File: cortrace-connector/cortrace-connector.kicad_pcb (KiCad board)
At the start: 2 copper layers, 8 parts, among them J1 FPGA-PORT, J2 Conn_ARM_Cortex_Debug_ETM_20, J4 SWD-PORT

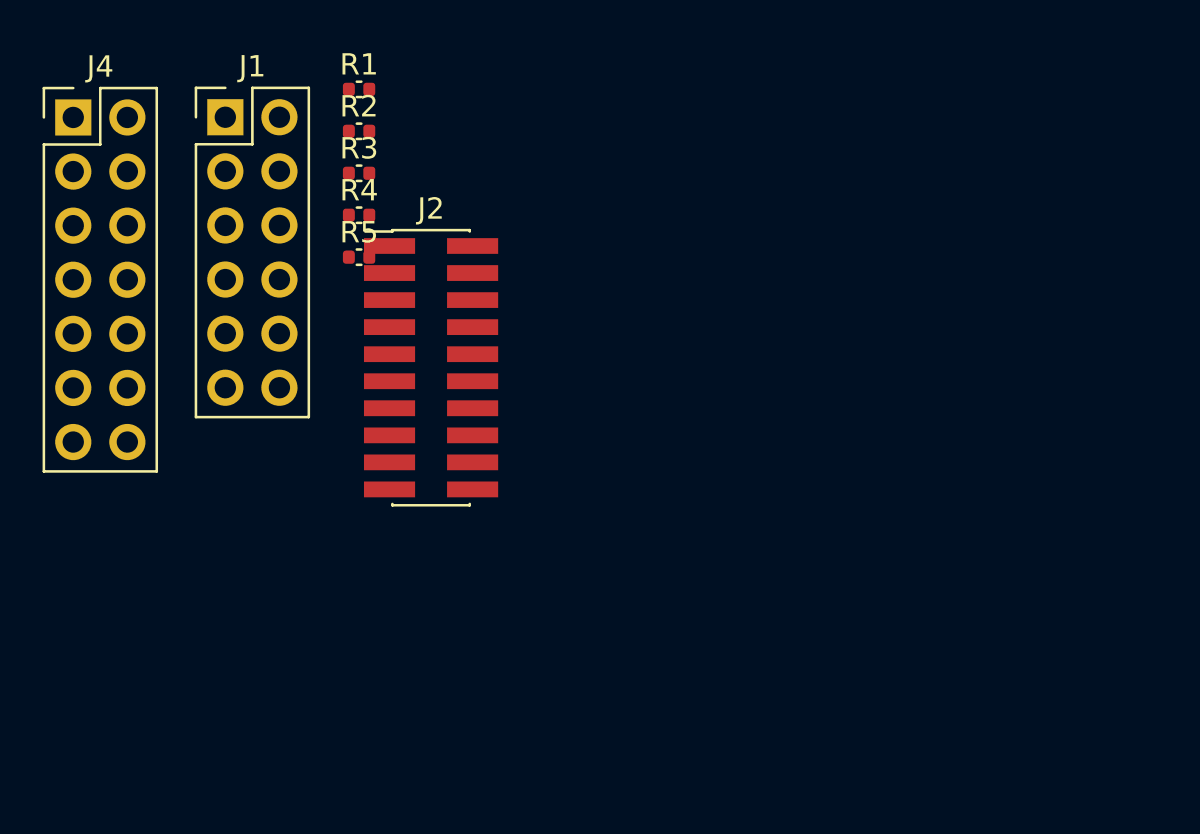
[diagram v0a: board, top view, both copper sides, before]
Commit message: feat(connector): lay out and route the adapter board
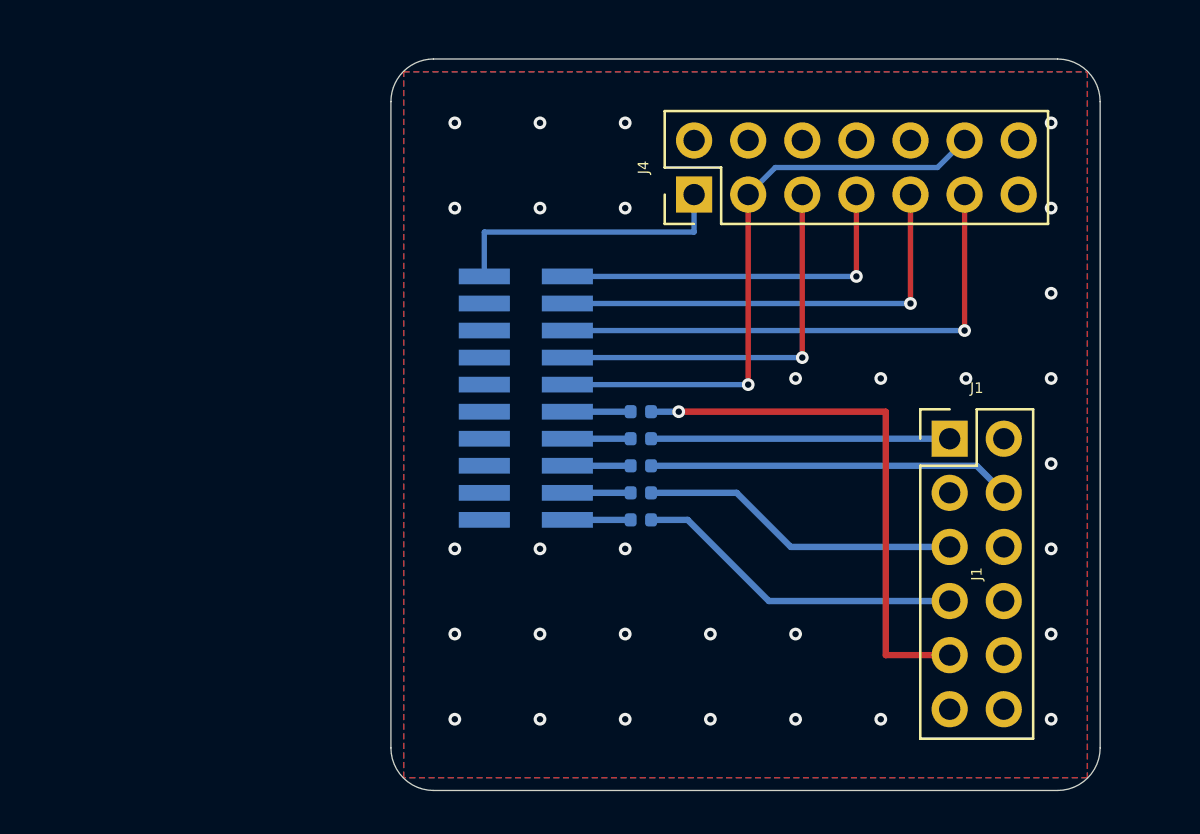
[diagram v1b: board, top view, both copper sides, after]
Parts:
- J2, R1, R2, R3, R4, R5: moved to B.Cu
- moved J1 37.2 mm to (140.0, 81.9)
- moved J4 29.4 mm to (128.0, 70.4), turned to 90 degrees
- moved R1 20.1 mm to (125.5, 80.6)
- moved R2 19.6 mm to (125.5, 81.9)
- moved R3 19.1 mm to (125.5, 83.2)
- moved R4 18.6 mm to (125.5, 84.4)
- moved R5 18.1 mm to (125.5, 85.7)
- moved J2 4.67 mm to (120.1, 80.0), turned to 180 degrees
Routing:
- net /NRST: track 0.00 -> 28.6 mm, vias 0 -> 1
- net /TRACE-CLK: track 0.00 -> 25.4 mm, vias 0 -> 1
- net /TDO: track 0.00 -> 25.0 mm, vias 0 -> 1
- net /TCK: track 0.00 -> 21.2 mm, vias 0 -> 1
- net /TDI: track 0.00 -> 18.7 mm, vias 0 -> 1
- net /TMS: track 0.00 -> 17.4 mm, vias 0 -> 1
- net /TRACE-D1: track 0.00 -> 17.1 mm
- net /TRACE-D3: track 0.00 -> 15.6 mm
- net /TRACE-D2: track 0.00 -> 15.1 mm
- net /TRACE-D0: track 0.00 -> 14.0 mm
- net /VREF: track 0.00 -> 13.7 mm
- net Net-(J2-TRACEDATA3): track 0.00 -> 2.97 mm
- net Net-(J2-TRACEDATA2): track 0.00 -> 2.97 mm
- net Net-(J2-TRACEDATA1): track 0.00 -> 2.97 mm
- net Net-(J2-TRACEDATA0): track 0.00 -> 2.97 mm
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- added copper zone on B.Cu, net GND
- added copper zone on F.Cu, net GND
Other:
- board outline added: 33.3 x 34.3 mm

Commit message: feat(connector): re-lay out the adapter board with arc routing
Import the board rules from DutyCycle, follow the sketched placement (TRACE socket left, JTAG and FPGA headers right), route every signal on B.Cu with arcs and no vias, add teardrops, GND pours, stitching vias and silkscreen (logo, author, revision, date, pin names).
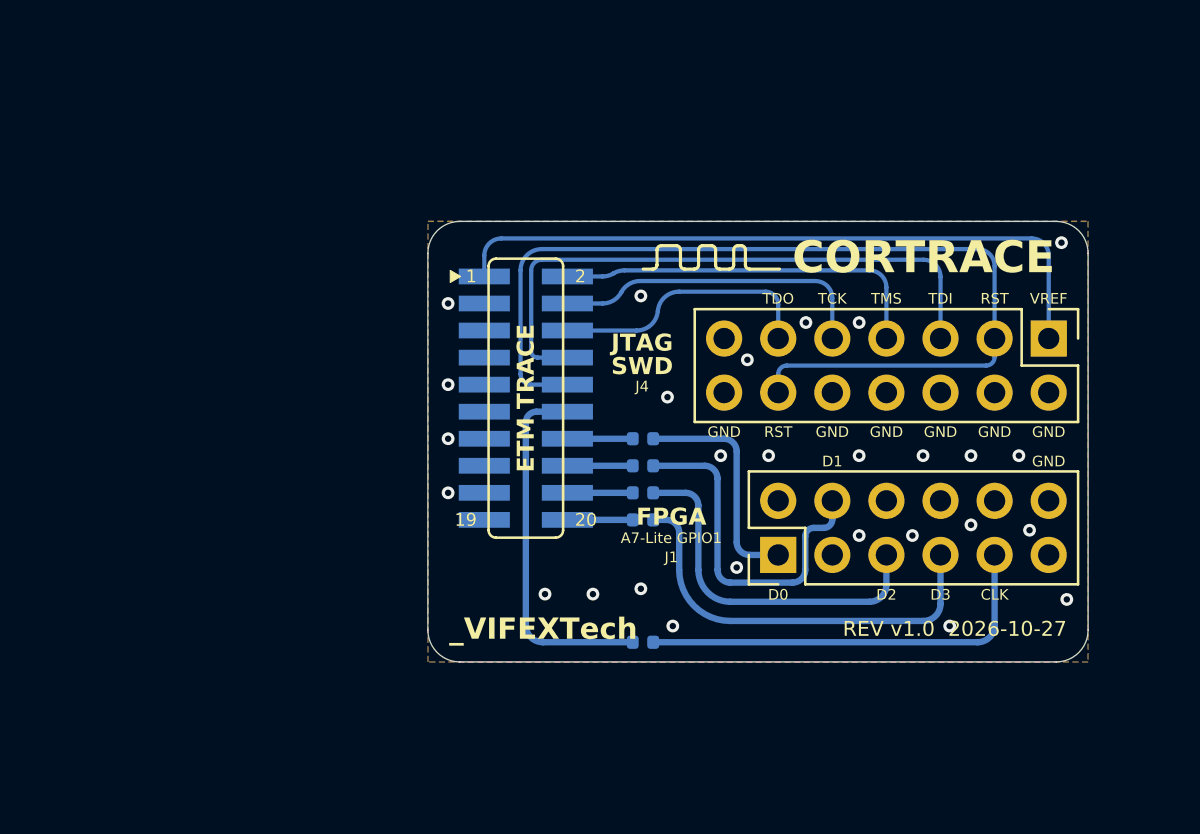
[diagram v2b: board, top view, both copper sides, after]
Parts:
- moved J4 18.0 mm to (144.7, 77.2), turned to -90 degrees
- moved R1 10.8 mm to (125.6, 91.5)
- moved J1 9.72 mm to (131.9, 87.4), turned to 90 degrees
- moved R2 0.10 mm to (125.6, 81.9)
- moved R3 0.10 mm to (125.6, 83.2)
- moved R4 0.10 mm to (125.6, 84.4)
- moved R5 0.10 mm to (125.6, 85.7)
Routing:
- net /VREF: track 13.7 -> 32.2 mm
- net /NRST: track 28.6 -> 46.3 mm, vias 1 -> 0
- net Net-(J2-TRACECLK): track 2.97 -> 17.2 mm
- net /TDO: track 25.0 -> 12.7 mm, vias 1 -> 0
- net /TDI: track 18.7 -> 28.5 mm, vias 1 -> 0
- net /TCK: track 21.2 -> 15.1 mm, vias 1 -> 0
- net /TRACE-CLK: track 25.4 -> 19.8 mm, vias 1 -> 0
- net /TRACE-D3: track 15.6 -> 19.6 mm
- net /TRACE-D0: track 14.0 -> 10.8 mm
- net /TRACE-D2: track 15.1 -> 16.9 mm
- net /TRACE-D1: track 17.1 -> 16.5 mm
- net /TMS: track 17.4 -> 17.9 mm, vias 1 -> 0
- net GND: vias 31 -> 27
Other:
- board size 33.3 x 34.3 mm -> 31 x 20.7 mm
- board text added: "1"
- board text added: "19"
- board text added: "2"
- board text added: "20"
- board text added: "A7-Lite GPIO1"
- board text added: "CLK"
- board text added: "CORTRACE"
- board text added: "D0"
- board text added: "D1"
- board text added: "D2"
- board text added: "D3"
- board text added: "ETM TRACE"
- board text added: "FPGA"
- board text added: "GND"
- board text added: "JTAG"
- board text added: "REV ${REVISION} ${ISSUE_DATE}"
- board text added: "RST"
- board text added: "SWD"
- board text added: "TCK"
- board text added: "TDI"
- board text added: "TDO"
- board text added: "TMS"
- board text added: "TRACE"
- board text added: "VREF"
- board text added: "_VIFEXTech"

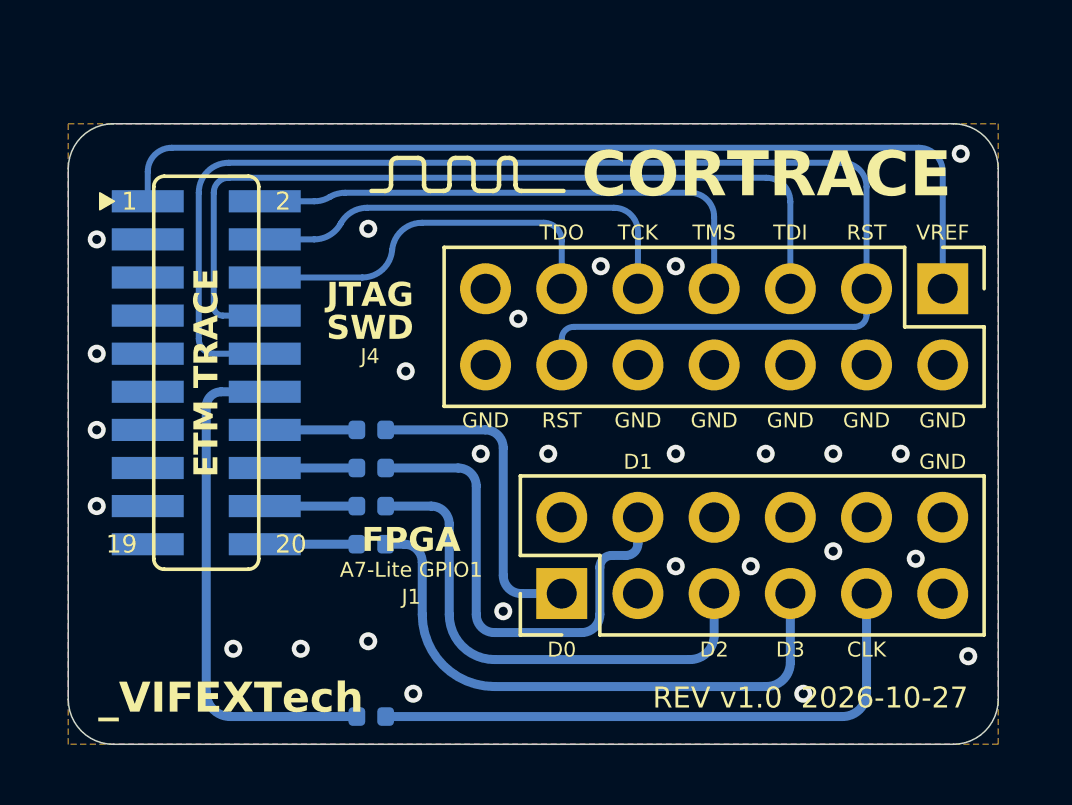
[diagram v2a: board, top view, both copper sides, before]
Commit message: feat(connector): length-match the TRACE nets and centre the board on J2
All five TRACE nets (J2 pad to J1 pad) are 24.174 mm. CLK now runs straight through the gap between the headers; D0..D3 are tuned with rounded bumps and a trombone, each in space only that net reaches. The outline is symmetric about the J2 centre.
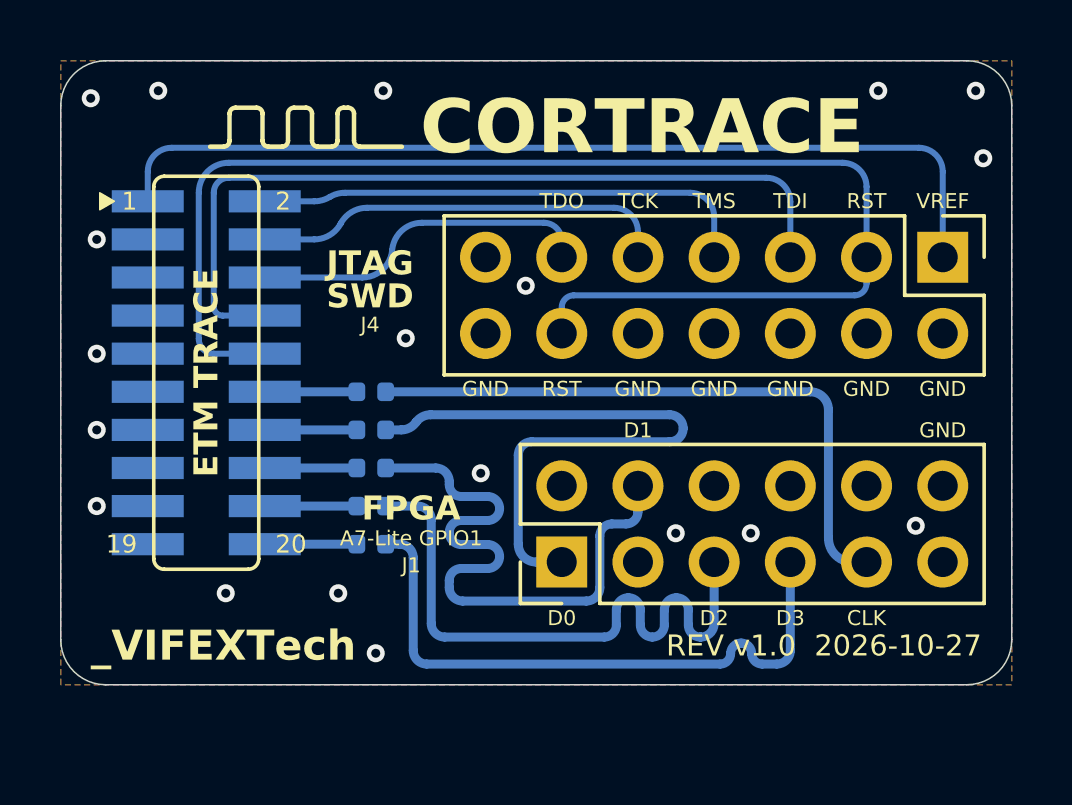
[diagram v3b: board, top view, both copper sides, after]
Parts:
- moved R1 10.8 mm to (125.6, 80.6)
- moved J1 1.05 mm to (131.9, 86.3)
- moved J4 1.05 mm to (144.7, 76.2)
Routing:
- net Net-(J2-TRACECLK): track 17.2 -> 3.07 mm
- net /TRACE-D0: track 10.8 -> 21.0 mm
- net /TRACE-D1: track 16.5 -> 20.9 mm
- net /TRACE-D2: track 16.9 -> 20.9 mm
- net /TRACE-D3: track 19.6 -> 21.0 mm
- net /TRACE-CLK: track 19.8 -> 21.0 mm
- net /TMS: track 17.9 -> 16.8 mm
- net /TDO: track 12.7 -> 11.7 mm
- net /TDI: track 28.5 -> 27.4 mm
- net /TCK: track 15.1 -> 14.1 mm
- net /VREF: track 32.2 -> 31.2 mm
- net /NRST: track 46.3 -> 45.2 mm
- net GND: vias 27 -> 19
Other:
- board size 31 x 20.7 mm -> 31.7 x 20.8 mm

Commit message: feat(connector): label the SWD pin names on the debug header
TMS/SWDIO, TCK/SWCLK and TDO/SWO share a pin each, so the silkscreen shows both names on two lines. VREF and RST apply to both modes.
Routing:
- net GND: vias 19 -> 18
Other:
- board text added: "SWCLK"
- board text added: "SWDIO"
- board text added: "SWO"

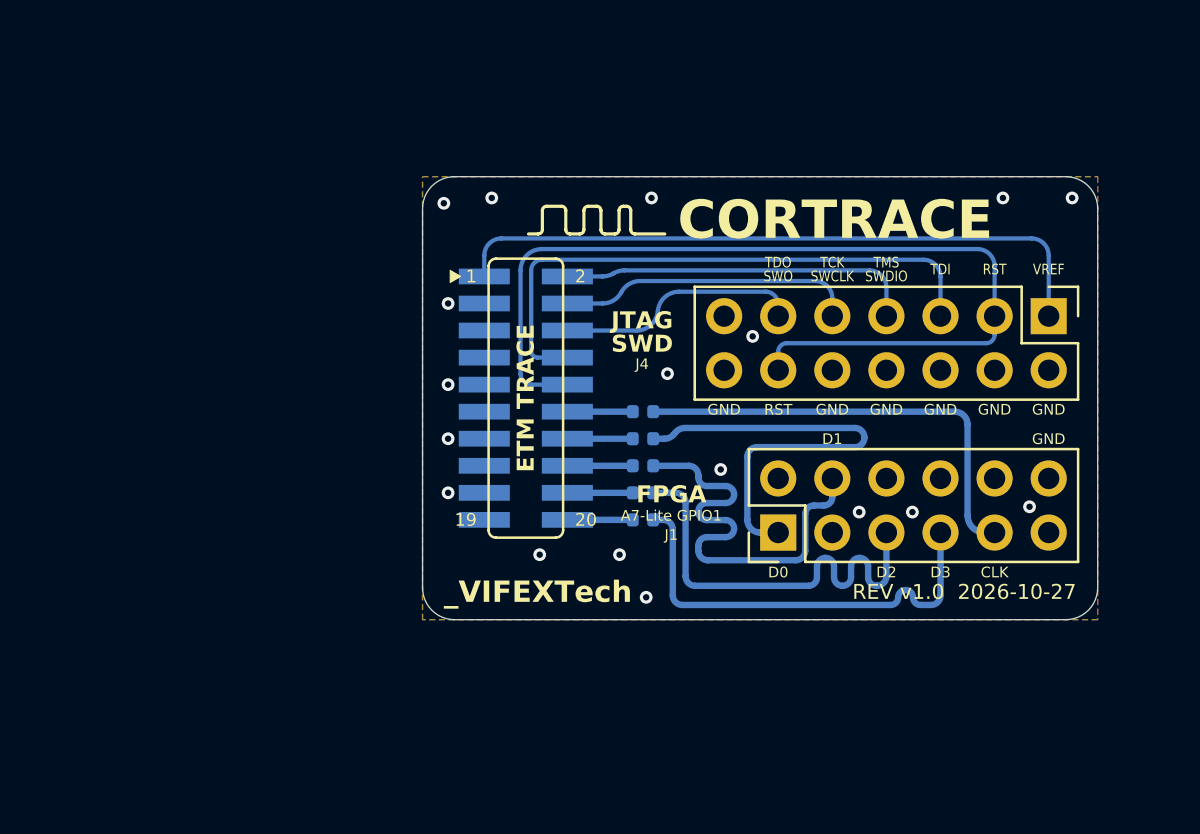
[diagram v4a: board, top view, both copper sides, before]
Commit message: feat(connector): widen TRACE spacing and pour GND between the lines
Differently-named TRACE nets now keep at least a 0.92 mm edge gap wherever they run side by side (was 0.3 mm in places), so a 0.6 mm GND strip is poured between them and tied to the top plane with shield vias. Lengths stay matched at 27.110 mm. Board is 34.5 x 22.0 mm.
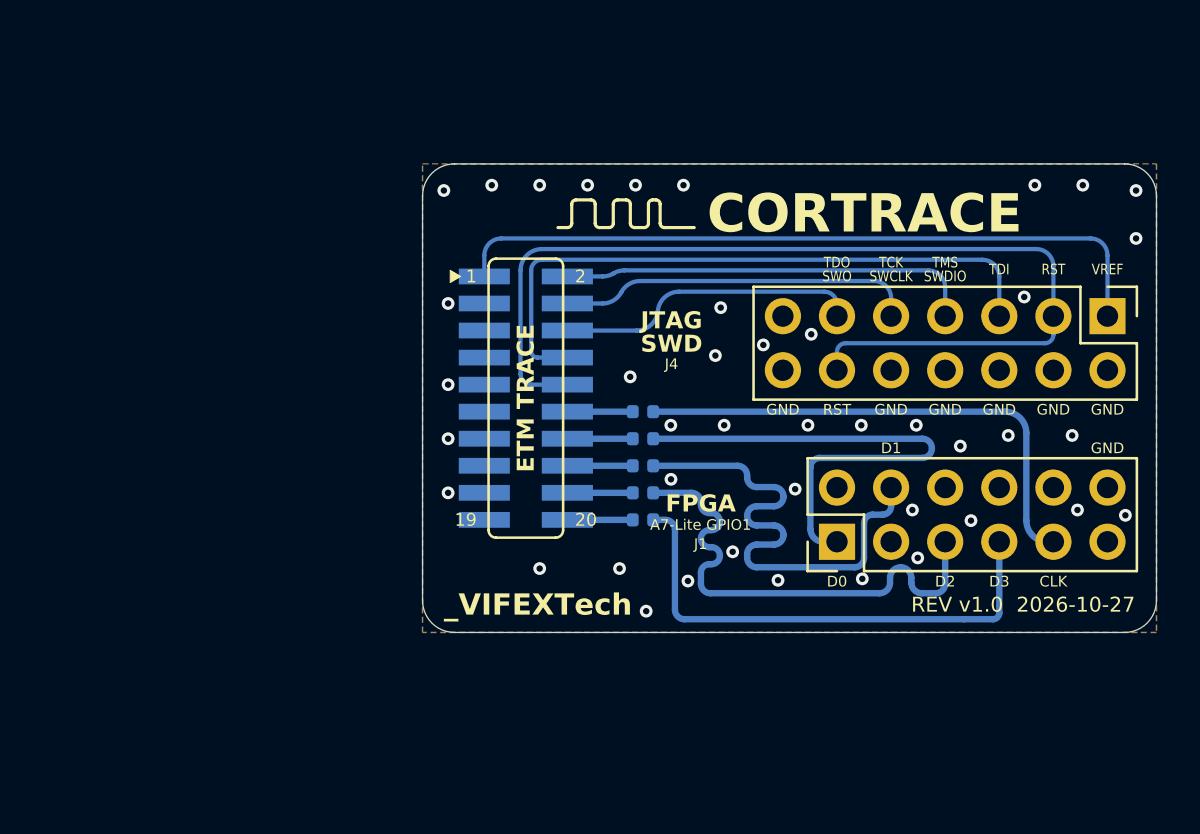
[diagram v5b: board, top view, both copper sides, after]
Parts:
- moved J1 2.79 mm to (134.7, 86.7)
- moved J4 2.76 mm to (147.4, 76.2)
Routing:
- net /TRACE-D3: track 21.0 -> 24.0 mm
- net /TRACE-D0: track 21.0 -> 24.0 mm
- net /TRACE-D1: track 20.9 -> 23.8 mm
- net /TRACE-CLK: track 21.0 -> 24.0 mm
- net /TRACE-D2: track 20.9 -> 23.8 mm
- net /TDO: track 11.7 -> 14.4 mm
- net /TMS: track 16.8 -> 19.6 mm
- net /TDI: track 27.4 -> 30.2 mm
- net /NRST: track 45.2 -> 48.0 mm
- net /VREF: track 31.2 -> 33.9 mm
- net /TCK: track 14.1 -> 16.8 mm
- net GND: vias 18 -> 42
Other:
- board size 31.7 x 20.8 mm -> 34.5 x 22 mm
